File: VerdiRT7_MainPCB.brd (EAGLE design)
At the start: 146 x 66 mm, 193 parts, among them J1 RECEPT_SMD_5-2, J13 DF58_2P, J15 503480_0400, J16 503480_0600, J2 RECEPT_SMD_5-2, J3 DF13-4P-1.25DSA, J4 MOLEX_105027, J6 52559-0652, J7 503480_1400, J8 BM02B-SRSS-TB, Q1 SIZ322DT, Q2 SIZ322DT, Q3 SIZ322DT, Q5 SIZ322DT, Q6 SIZ322DT, Q7 SI7615ADN, Q8 SIZ322DT, SW1 AYZ0102AGRLC, SW3 SKRH, SW4 TACT_SWITCHO, U10 RT9625A, U13 MCP1416, U14 MCP1416, U15 MCP1416, U16 MCP6001, U17 MCP6001, U18 RT9625A, U19 ICM-20602, U2 MR20H40, U3 7408_3, U4 RT9625A, U5 MCP6001, U6 MCP1416, U7 7408_3, U8 7408_3, U9 MCP6001, X1 NX3225

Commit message: updated: リナンバー完了，BOM 完了
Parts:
- removed C19, C30: 16V33u, capacitor:EEFCX_7343
- removed C32, C40: 16V 33u, capacitor:EEFCX_7343
- removed LED1, LED2, LED3, LED4, LED5, LED6, LED8: (no value), led:1608-OLI
- removed Q7: SI7615ADN, MOSFET:POWERPAK1212-8
- removed SW4: TACT_SWITCHO, switch:TACT_SWITCH-OLI
- removed U3, U7, U8: 7408_3, 74xx-eu:VSSOP8
- added C203, C206, C302, C315: EEF-CS1C330R, capacitor:EEFC_7343
- added LED101, LED102, LED103, LED104: APHHS1005QBC/D, LED:1005
- added LED201, LED203: APHHS1005SYCK, LED:1005
- added LED202: APHHS1005ZGC, LED:1005
- added Q201: SISA01DN-T1-GE3, MOSFET:POWERPAK1212-8
- added SW102: SKQYACE010, switch:SKQYA
- added U301, U303, U305: 74LVC2G08DC, 74xx-eu:VSSOP8
- B101: value SMT-0540-S-R -> SMT-0540-T-7-R
- J102: value (none) -> BM04B-SRSS-TB(LF)(SN)
- J104: value MOLEX_105027 -> 1050270001
- J201: value DF58_2P -> DF58-2P-1.2V(21)
- J301, J302: value RECEPT_SMD_5-2 -> 20021321-00010C4LF
- J303: value BM02B-SRSS-TB -> BM02B-SRSS-TB(LF)(SN)
- Q301, Q302, Q303, Q304, Q305, Q306: value SIZ322DT -> SIZ322DT-T1-GE3
- R113, R114: value 20k -> 20k (DNP)
- R117, R118, R123: value 22 -> 22 (DNP)
- R140: value 100k -> 100k (DNP)
- SW101: value SKRH -> SKRHABE010
- U101, U401, U403, U404: value MCP1416 -> MCP1416T-E/OT
- U102, U103, U402, U405: value MCP6001 -> MCP6001T-I/LT
- U104: value (none) -> R5F564MLDDFP#V1-ND
- U105: value MR20H40 -> MR20H40CDF
- U201: value (none) -> TLV1117-50CDRJR
- U202: value (none) -> TLV1117-33CDRJR
- U302, U304, U306: value RT9625A -> RT9625AZQW
- VR101: value SV01 -> SV01A103AEA01
- X101: value NX3225 -> NX3225SA-12.000M-STD-CSR-1
- renumbered B1 to B101, C1 to C204, C10 to C501, C11 to C314, C12 to C201, C13 to C316, C14 to C310, C15 to C104, C16 to C103, C17 to C102, C18 to C106, C2 to C317, C20 to C313, C21 to C502, C22 to C117, C23 to C112, C24 to C113, C25 to C108, C26 to C504, C27 to C111, C28 to C309, C29 to C311, C3 to C115, C31 to C312, C33 to C303, C34 to C307, C35 to C301, C36 to C304, C37 to C205, C38 to C202, C39 to C306, C4 to C406, C41 to C114, C42 to C503, C43 to C119, C44 to C401, C45 to C404, C46 to C405, C47 to C107, C48 to C110, C49 to C403, C5 to C318, C50 to C407, C51 to C101, C52 to C408, C53 to C109, C54 to C105, C55 to C120, C56 to C118, C57 to C116, C6 to C402, C7 to C305, C8 to C308, C9 to C319, D1 to D101, D2 to D102, J1 to J302, J11 to J102, J13 to J201, J15 to J105, J16 to J106, J2 to J301, J3 to J103, J4 to J104, J6 to J401, J7 to J101, J8 to J303, PI1 to PI401, PI2 to PI402, Q1 to Q305, Q2 to Q306, Q3 to Q302, Q5 to Q301, Q6 to Q303, Q8 to Q304, R1 to R110, R10 to R309, R11 to R311, R12 to R111, R13 to R104, R14 to R107, R15 to R314, R16 to R315, R17 to R317, R18 to R136, R19 to R404, R2 to R324, R20 to R112, R21 to R109, R22 to R108, R23 to R330, R24 to R327, R25 to R329, R26 to R325, R27 to R318, R28 to R323, R29 to R331, R3 to R502, R30 to R124, R31 to R128, R32 to R319, R33 to R316, R34 to R321, R35 to R320, R36 to R322, R37 to R313, R38 to R303, R39 to R312, R4 to R326, R40 to R302, R41 to R125, R42 to R203, R43 to R202, R44 to R306, R45 to R201, R46 to R304, R47 to R310, R48 to R301, R49 to R401, R5 to R103, R50 to R402, R51 to R403, R52 to R405, R53 to R204, R54 to R101, R55 to R105, R56 to R106, R57 to R102, R58 to R120, R59 to R119, R6 to R305, R60 to R116, R61 to R115, R62 to R137, R63 to R501, R64 to R131, R65 to R138, R66 to R129, R67 to R133, R68 to R132, R69 to R135, R7 to R328, R70 to R122, R70(DNP) to R123, R71 to R121, R71(DNP) to R117, R72 to R126, R72(DNP) to R118, R73 to R127, R73_ to R139, R74 to R130, R74(DNP) to R140, R75 to R134, R75(DNP) to R114, R76(DNP) to R113, R8 to R307, R9 to R308, SW1 to SW201, SW3 to SW101, U1 to U104, U10 to U302, U11 to U201, U12 to U202, U13 to U404, U14 to U401, U15 to U403, U16 to U402, U17 to U405, U18 to U306, U19 to U501, U2 to U105, U4 to U304, U5 to U103, U6 to U101, U9 to U102, VR1 to VR101, X1 to X101
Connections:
- net AD_ASEN1 renamed AD_LINE_L_SEN
- net AD_ASEN2 renamed AD_LINE_R_SEN
- net AD_DSEN1 renamed AD_MARKER_L_SEN
- net AD_DSEN2 renamed AD_MARKER_R_SEN
- net MOTOR7 renamed DRIVE_MOTOR_EN
- net MOTOR8 renamed SENSOR_MOTOR_EN
- net TCLK1 renamed RIGHT_TCLKA
- net TCLK2 renamed RIGHT_TCLKB
- net TCLK3 renamed LEFT_TCLKC
- net TCLK4 renamed LEFT_TCLKD
- removed net MOTOR1: U104.86, U7.1
- removed net MOTOR2: U104.85, U7.6
- removed net MOTOR3: U104.78, U3.1
- removed net MOTOR4: U104.75, U3.6
- removed net MOTOR5: U104.74, U8.1
- removed net MOTOR6: U104.61, U8.6
- removed net PWM_MOTOR1: R137.P$1, U7.2, U7.5
- removed net PWM_MOTOR2: R138.P$1, U3.2, U3.5
- removed net PWM_MOTOR3: R129.P$1, U8.2, U8.5
- new net LEFT_MOTOR_CCW: U104.86, U301.1
- new net LEFT_MOTOR_CW: U104.85, U301.6
- new net LEFT_MOTOR_PWM: R137.P$1, U301.2, U301.5
- new net RIGHT_MOTOR_CCW: U104.78, U303.1
- new net RIGHT_MOTOR_CW: U104.75, U303.6
- new net RIGHT_MOTOR_PWM: R138.P$1, U303.2, U303.5
- new net SENSOR_MOTOR_CCW: U104.74, U305.1
- new net SENSOR_MOTOR_CW: U104.61, U305.6
- new net SENSOR_MOTOR_PWM: R129.P$1, U305.2, U305.5
- net +3V3: now also C206.PLUS, U301.8, U303.8, U305.8; no longer C19.PLUS, U3.8, U7.8, U8.8
- net +5V: now also C203.PLUS; no longer C30.PLUS
- net +8V: now also C302.PLUS, C315.PLUS, Q201.5, Q201.9; no longer C32.PLUS, C40.PLUS, Q7.5, Q7.9
- net GND: now also C203.MINUS, C206.MINUS, C302.MINUS, C315.MINUS, LED201.K, LED202.K, LED203.K, SW102.2, U301.4, U303.4, U305.4; no longer C19.MINUS, C30.MINUS, C32.MINUS, C40.MINUS, LED4.K, LED5.K, LED8.K, SW4.2, U3.4, U7.4, U8.4
- net LED0: now also LED101.K; no longer LED1.K
- net LED1: now also LED102.K; no longer LED2.K
- net LED2: now also LED103.K; no longer LED3.K
- net LED3: now also LED104.K; no longer LED6.K
- net N$1: now also Q201.4; no longer Q7.4
- net N$12: now also LED201.A; no longer LED4.A
- net N$3: now also LED202.A; no longer LED5.A
- net N$31: now also U303.7; no longer U3.7
- net N$33: now also U303.3; no longer U3.3
- net N$49: now also U301.7; no longer U7.7
- net N$50: now also U301.3; no longer U7.3
- net N$56: now also LED101.A; no longer LED1.A
- net N$57: now also LED102.A; no longer LED2.A
- net N$58: now also LED103.A; no longer LED3.A
- net N$59: now also LED104.A; no longer LED6.A
- net N$70: now also U305.7; no longer U8.7
- net N$71: now also U305.3; no longer U8.3
- net N$78: now also LED203.A; no longer LED8.A
- net RESET: now also SW102.1; no longer SW4.1
- net VCC: now also Q201.1; no longer Q7.1
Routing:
- net MOTOR2: track 50.3 -> 0.00 mm, vias 5 -> 0
- net LEFT_MOTOR_CW: track 0.00 -> 50.3 mm, vias 0 -> 5
- net LEFT_MOTOR_CCW: track 0.00 -> 49.5 mm, vias 0 -> 5
- net MOTOR1: track 49.4 -> 0.00 mm, vias 5 -> 0
- net SENSOR_MOTOR_PWM: track 0.00 -> 43.2 mm, vias 0 -> 4
- net PWM_MOTOR3: track 43.2 -> 0.00 mm, vias 4 -> 0
- net PWM_MOTOR1: track 40.0 -> 0.00 mm, vias 4 -> 0
- net LEFT_MOTOR_PWM: track 0.00 -> 39.4 mm, vias 0 -> 4
- net SENSOR_MOTOR_CW: track 0.00 -> 31.4 mm, vias 0 -> 3
- net MOTOR6: track 31.4 -> 0.00 mm, vias 3 -> 0
- net MOTOR5: track 22.8 -> 0.00 mm, vias 3 -> 0
- net SENSOR_MOTOR_CCW: track 0.00 -> 22.8 mm, vias 0 -> 3
- net RIGHT_MOTOR_CW: track 0.00 -> 18.2 mm, vias 0 -> 1
- net MOTOR4: track 17.9 -> 0.00 mm, vias 1 -> 0
- net RIGHT_MOTOR_PWM: track 0.00 -> 16.0 mm, vias 0 -> 1
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
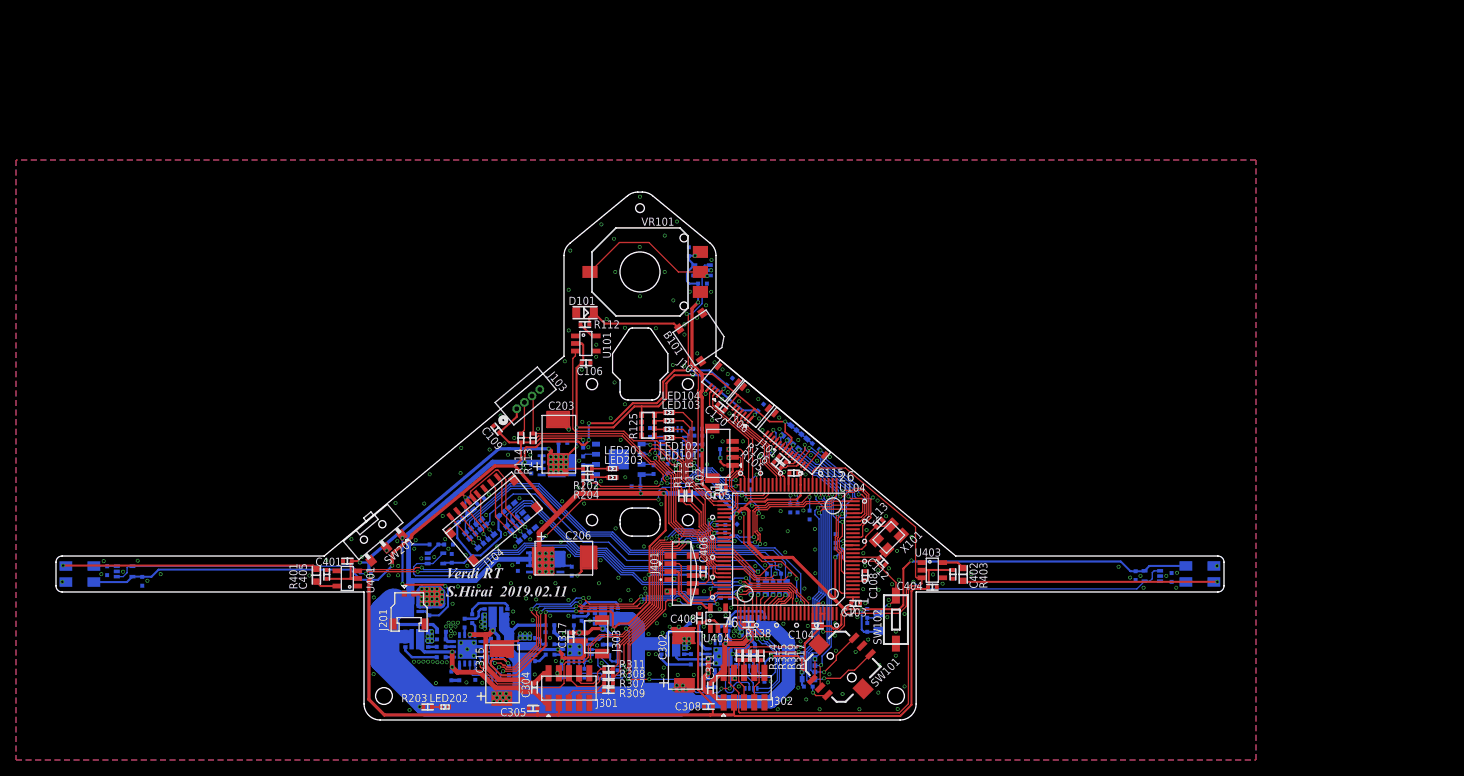
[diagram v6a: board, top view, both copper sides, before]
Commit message: updated: 捨て基板や認識マークを追加．発注データ作成
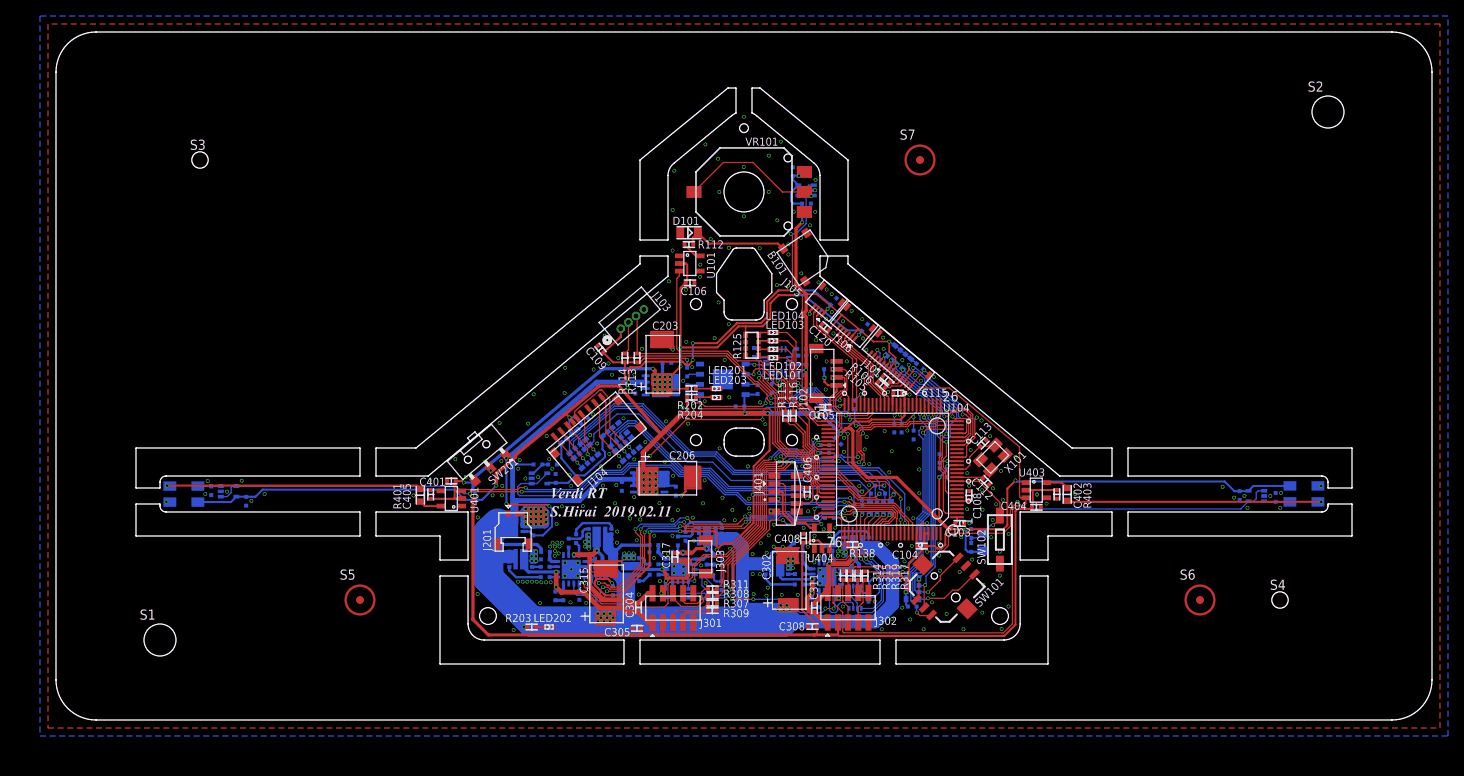
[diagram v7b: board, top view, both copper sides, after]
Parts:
- added S1, S2: BASE_HOLE, MountingSymbol:BASE_HOLE
- added S3: GUIDE_HOLE_1, MountingSymbol:GUIDE_HOLE
- added S4: GUIDE_HOLE_2, MountingSymbol:GUIDE_HOLE
- added S5: RECOG_MARK_1, MountingSymbol:RECOG_MARK
- added S6: RECOG_MARK_2, MountingSymbol:RECOG_MARK
- added S7: RECOG_MARK_3, MountingSymbol:RECOG_MARK
- moved U201 16.4 mm to (75.6, 41.8)
- moved C110 16.4 mm to (92.1, 68.5)
- moved C206 16.4 mm to (76.5, 30.2)
- moved Q306 16.4 mm to (71.9, 18.8)
- moved R305 16.4 mm to (65.4, 15.6)
- moved U103 16.4 mm to (93.8, 66.2)
- moved U301 16.4 mm to (67.8, 16.5)
- moved C116 16.4 mm to (85.5, 39.2)
- moved C316 16.4 mm to (82.3, 20.0)
- moved D102 16.4 mm to (115.9, 22.3)
- moved J201 16.4 mm to (57.1, 23.6)
- moved Q302 16.4 mm to (58.1, 20.1)
- moved Q303 16.4 mm to (100.2, 21.9)
- moved R140 16.4 mm to (110.4, 32.7)
- moved R202 16.4 mm to (79.4, 41.4)
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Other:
- board size 146 x 66 mm -> 172 x 86 mm
